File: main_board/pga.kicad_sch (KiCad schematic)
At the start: 0 parts

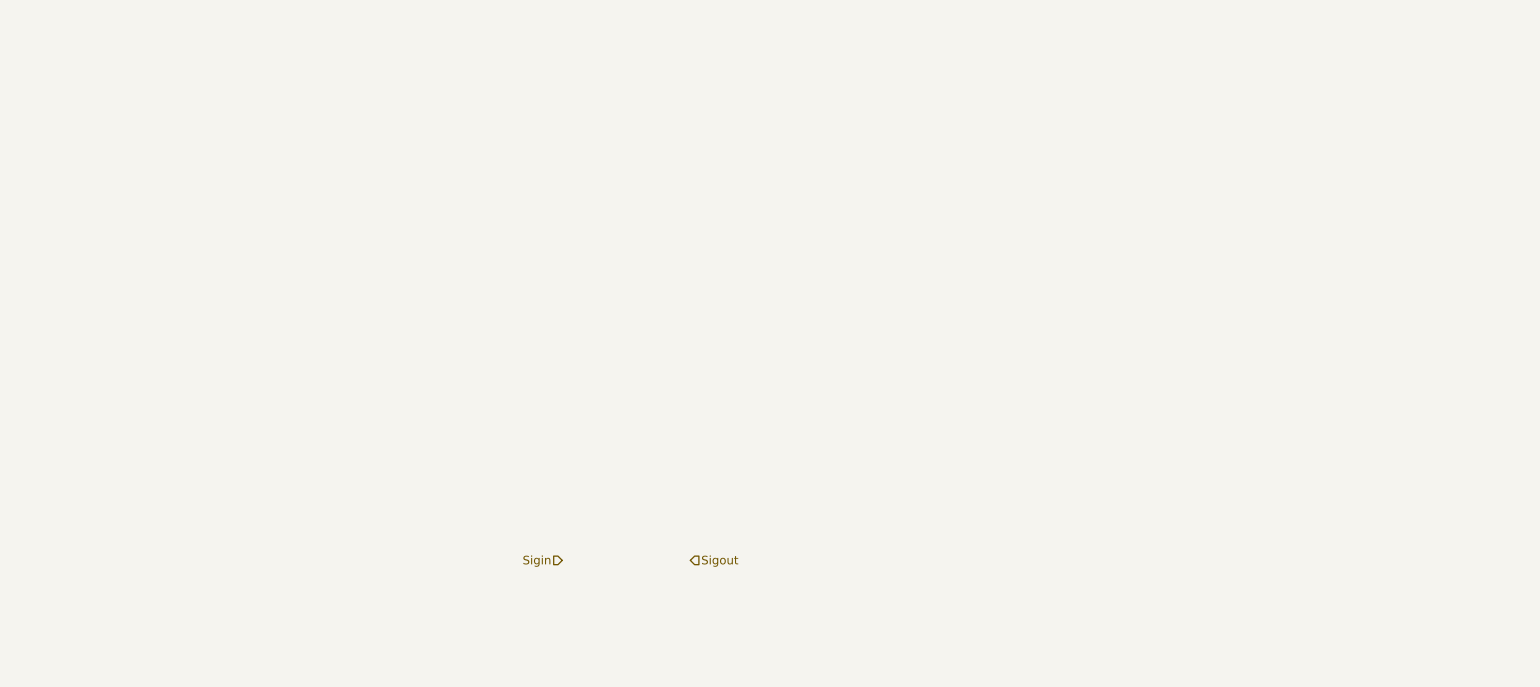
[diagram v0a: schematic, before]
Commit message: implemented PGA, wrote TODOS, connected blocks in root
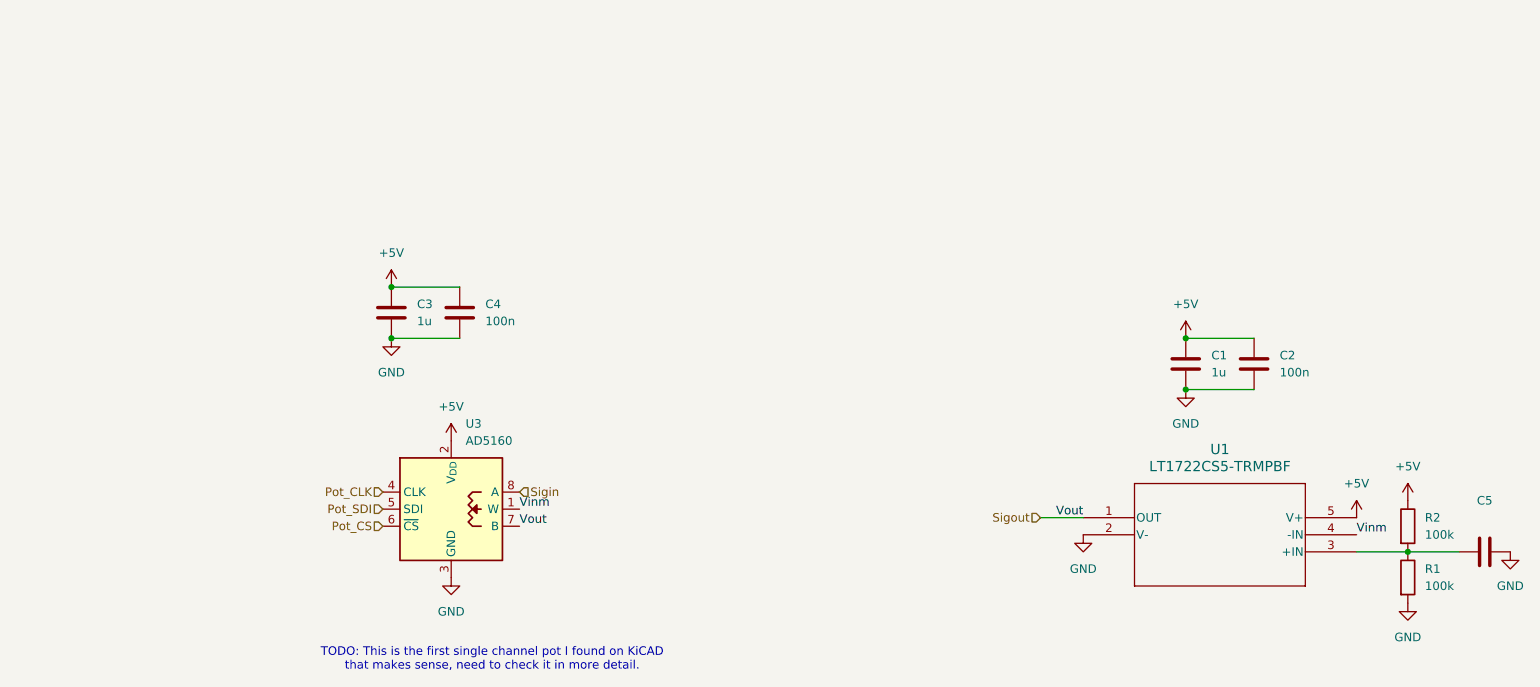
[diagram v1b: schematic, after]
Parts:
- added C1, C3: 1u, symbol Device:C
- added C2, C4: 100n, symbol Device:C
- added C5: ~, symbol Device:C
- added R1, R2: 100k, symbol Device:R
- added U1: LT1722CS5-TRMPBF, S_5_ADI, symbol LT172x:LT1722CS5-TRMPBF
- added U3: AD5160, Package_TO_SOT_SMD:SOT-23-8, symbol Potentiometer_Digital:AD5160
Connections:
- net Sigin: now also U3.8 (A)
- net Sigout: now also U1.1 (OUT), U3.7 (B)
- new net: C5.1, R1.1, R2.2, U1.3 (+IN)
- new net +5V: C1.1, C2.1, C3.1, C4.1, R2.1, U1.5 (V+), U3.2 (V_{DD})
- new net GND: C1.2, C2.2, C3.2, C4.2, C5.2, R1.2, U1.2 (V-), U3.3 (GND)
- new net Pot_CLK: U3.4 (CLK)
- new net Pot_CS: U3.6 (~{CS})
- new net Pot_SDI: U3.5 (SDI)
- new net Vinm: U1.4 (-IN), U3.1 (W)
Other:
- note added: "TODO: This is the first single channel pot I found on KiCAD that makes sense, need to check it in more detail."

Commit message: update power supply decoupling caps
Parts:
- removed C1: 1u, symbol Device:C
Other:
- note added: "One bulk cap, one 100n for each IC"
- moved on the sheet: C2, C3, C4

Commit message: remove todo
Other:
- note removed: "TODO: This is the first single channel pot I found on KiCAD that makes sense, need to check it in more detail."
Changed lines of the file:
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@@
-		)
-	)
-	(text "TODO: This is the first single channel pot I found on KiCAD\nthat makes sense, need to check it in more detail."
-		(exclude_from_sim no)
-		(at 97.536 117.602 0)
-		(effects
-			(font
-				(size 1.27 1.27)
-			)
 		)
 	)

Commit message: Added PCBway drc ruleset, connected mux IO, ADC SPI interface, Pot SPI interface & 0603 footprints to all passive devices.
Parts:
- C2, C3, C4, C5: footprint (none) -> Capacitor_SMD:C_0603_1608Metric
- R1, R2: footprint (none) -> Resistor_SMD:R_0603_1608Metric
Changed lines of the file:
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@@
 			)
 		)
-		(property "Footprint" ""
+		(property "Footprint" "Capacitor_SMD:C_0603_1608Metric"
 			(at 248.92 100.6348 0)
 			(effects
@@
 			)
 		)
-		(property "Footprint" ""
+		(property "Footprint" "Capacitor_SMD:C_0603_1608Metric"
 			(at 59.3852 35.56 0)
 			(effects
@@
 			)
 		)
-		(property "Footprint" ""
+		(property "Footprint" "Capacitor_SMD:C_0603_1608Metric"
 			(at 36.5252 35.56 0)
 			(effects
@@
 			)
 		)
-		(property "Footprint" ""
+		(property "Footprint" "Capacitor_SMD:C_0603_1608Metric"
 			(at 46.6852 35.56 0)
 			(effects
@@
 			)
 		)
-		(property "Footprint" ""
+		(property "Footprint" "Resistor_SMD:R_0603_1608Metric"
 			(at 231.902 97.79 90)
 			(effects
@@
 			)
 		)
-		(property "Footprint" ""
+		(property "Footprint" "Resistor_SMD:R_0603_1608Metric"
 			(at 231.902 105.41 90)
 			(effects

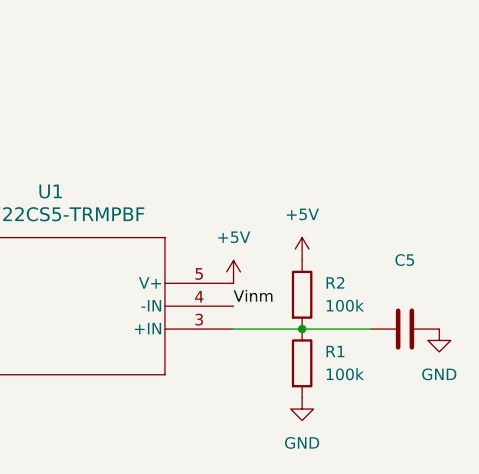
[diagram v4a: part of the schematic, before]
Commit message: add value for pga cap
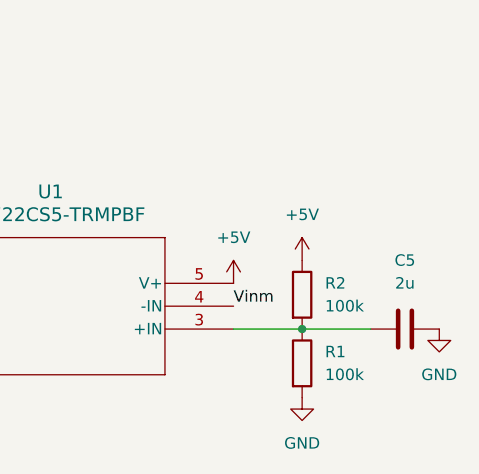
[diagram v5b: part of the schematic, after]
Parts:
- C5: value ~ -> 2u
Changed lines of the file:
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@@
 			)
 		)
-		(property "Value" "~"
+		(property "Value" "2u"
 			(at 245.11 96.52 90)
 			(effects

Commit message: Finalized last schematic changes, awaing group approval.
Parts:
- C5: value 2u -> .2u
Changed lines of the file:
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@@
 			)
 		)
-		(property "Value" "2u"
+		(property "Value" ".2u"
 			(at 245.11 96.52 90)
 			(effects

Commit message: fix schematic parity warnings by providing full path to footprint
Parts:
- U1: footprint S_5_ADI -> LT172x:S_5_ADI
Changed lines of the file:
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@@
 			)
 		)
-		(property "Footprint" "S_5_ADI"
+		(property "Footprint" "LT172x:S_5_ADI"
 			(at 206.375 105.41 0)
 			(effects
